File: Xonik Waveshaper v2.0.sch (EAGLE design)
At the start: 89 parts, among them IC1 TL074D, IC2 TL074D, IC3 TL074D, IC4 TL072D, IC5 4013D, T1 2n3904

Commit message: Silk screen tweak
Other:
- note added: "Max power: 1.5k/15k amp config: Clips long before input reaches +/-15V, max current when feeding into a 10k resistor is 800uA = 640uW. ok with 1/10w resistors"
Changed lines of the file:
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@@
 half the spike, but also rounds off the
 rest. Not sure if it is worth doing.</text>
+<text x="124.46" y="-10.16" size="1.778" layer="97">Max power:
+1.5k/15k amp config:
+Clips long before input reaches +/-15V,
+max current when feeding into a 10k resistor is
+800uA = 640uW.
+ok with 1/10w resistors</text>
 </plain>
 <instances>

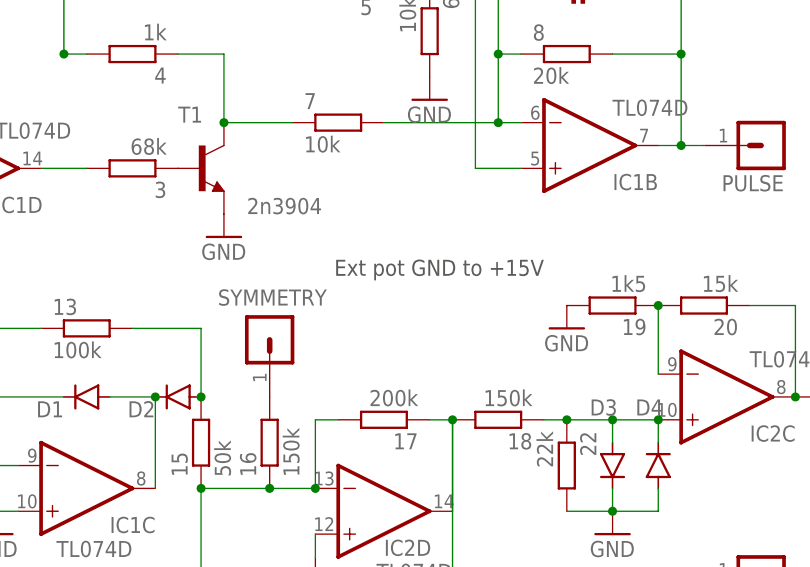
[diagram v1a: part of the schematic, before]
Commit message: Added info about trimmer value
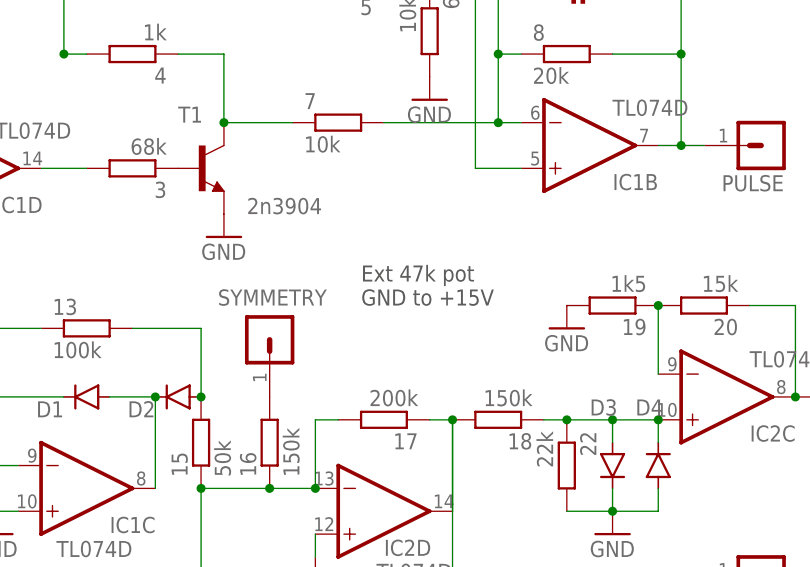
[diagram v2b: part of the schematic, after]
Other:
- note added: "Ext 47k pot GND to +15V"
- note removed: "Ext pot GND to +15V"
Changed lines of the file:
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@@
 <text x="129.54" y="22.86" size="1.778" layer="97">All caps 100nF</text>
 <text x="-48.26" y="27.94" size="1.778" layer="97">Ext 100k pot to -15V</text>
-<text x="73.66" y="73.66" size="1.778" layer="97" rot="R180">Ext pot GND to +15V</text>
+<text x="53.34" y="68.58" size="1.778" layer="97">Ext 47k pot
+GND to +15V</text>
 <text x="43.18" y="-22.86" size="1.778" layer="97" rot="R180">Ext 100k pot</text>
 <text x="43.18" y="-88.9" size="1.778" layer="97" rot="R180">Ext 100k pot</text>

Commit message: Added bom and gerber
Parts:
- C7: value 5pF -> 6pF
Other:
- note added: "used to be 5pF but 5p is extended part, using 6p instead."
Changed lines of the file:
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@@
 <part name="C5" library="resistor" deviceset="C-EU" device="C0805" value="100nF"/>
 <part name="C6" library="resistor" deviceset="C-EU" device="C0805" value="100nF"/>
-<part name="C7" library="resistor" deviceset="C-EU" device="C0805" value="5pF"/>
+<part name="C7" library="resistor" deviceset="C-EU" device="C0805" value="6pF"/>
 <part name="GND13" library="supply1" deviceset="GND" device=""/>
 <part name="55" library="resistor" deviceset="R-EU_" device="R0805" value="20k"/>
@@
 800uA = 640uW.
 ok with 1/10w resistors</text>
+<text x="76.2" y="114.3" size="2.54" layer="97">used to be 5pF but 5p
+is extended part, using 6p instead.</text>
 </plain>
 <instances>
@@
 <wire x1="50.8" y1="-124.46" x2="50.8" y2="-114.3" width="0.1524" layer="91"/>
 <pinref part="IC3" gate="A" pin="-IN"/>
-<wire x1="50.8" y1="-114.3" x2="50.8" y2="-104.14" width="0.1524" layer="91"/>
 <wire x1="50.8" y1="-104.14" x2="55.88" y2="-104.14" width="0.1524" layer="91"/>
 <wire x1="58.42" y1="-104.14" x2="55.88" y2="-104.14" width="0.1524" layer="91"/>
